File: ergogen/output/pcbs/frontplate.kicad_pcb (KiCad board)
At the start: 2 copper layers, 133.7 x 92.5 mm, 0 parts

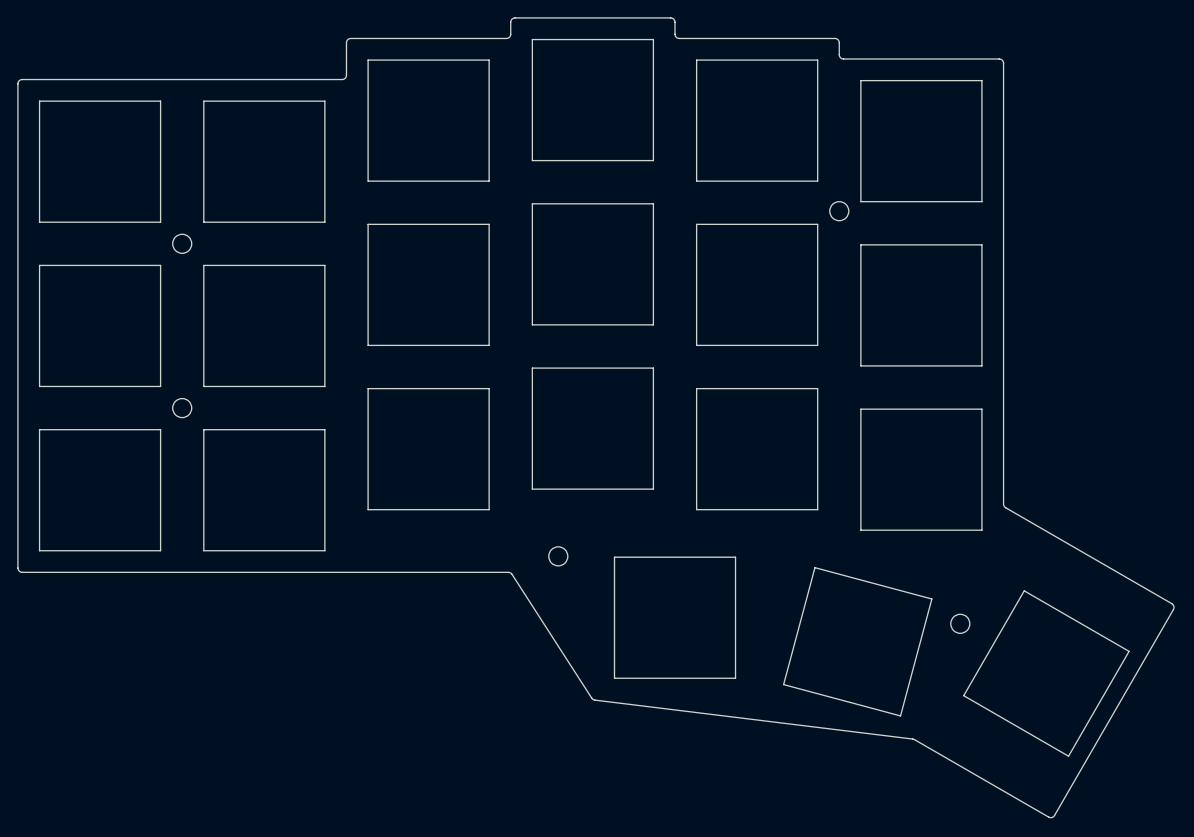
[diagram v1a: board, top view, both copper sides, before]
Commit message: Fix key positions to exactly match the corne
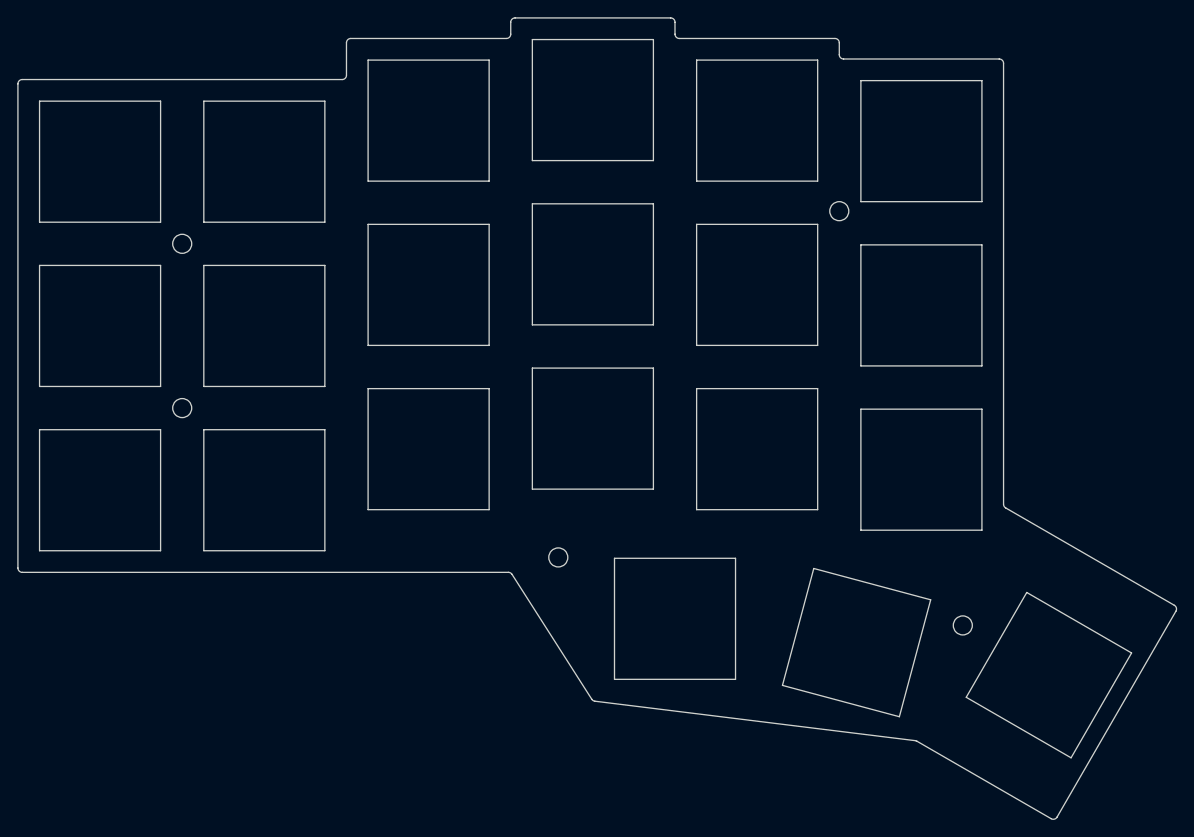
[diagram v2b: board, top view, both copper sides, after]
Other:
- board size 133.7 x 92.5 mm -> 134 x 92.7 mm
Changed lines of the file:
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@@
     (add_net "")
   )
-            (gr_line (start 91 109.5) (end 147.22730215593222 109.5) (angle 90) (layer Edge.Cuts) (width 0.15))
+            (gr_line (start 91 109.5) (end 147.226056907563 109.5) (angle 90) (layer Edge.Cuts) (width 0.15))
 (gr_line (start 90.5 109) (end 90.5 53) (angle 90) (layer Edge.Cuts) (width 0.15))
 (gr_line (start 91 52.5) (end 128 52.5) (angle 90) (layer Edge.Cuts) (width 0.15))
@@
 (gr_line (start 185.5 49.625) (end 185.5 48.25) (angle 90) (layer Edge.Cuts) (width 0.15))
 (gr_line (start 185 47.75) (end 167 47.75) (angle 90) (layer Edge.Cuts) (width 0.15))
-(gr_line (start 204.5 101.59766889781217) (end 204.5 50.625) (angle 90) (layer Edge.Cuts) (width 0.15))
+(gr_line (start 204.5 101.61675503683294) (end 204.5 50.625) (angle 90) (layer Edge.Cuts) (width 0.15))
 (gr_line (start 204 50.125) (end 186 50.125) (angle 90) (layer Edge.Cuts) (width 0.15))
-(gr_line (start 210.3979412988017 137.62313710032112) (end 224.14794130032098 113.80743850119836) (angle 90) (layer Edge.Cuts) (width 0.15))
-(gr_line (start 204.75 102.03068159781219) (end 223.96492860032103 113.12442580119826) (angle 90) (layer Edge.Cuts) (width 0.15))
-(gr_line (start 194.19299154809863 128.84455526290066) (end 209.71492859880163 137.80614980032107) (angle 90) (layer Edge.Cuts) (width 0.15))
-(gr_line (start 147.6476597559322 109.72926120000002) (end 156.8730776751543 124.05293639037114) (angle 90) (layer Edge.Cuts) (width 0.15))
-(gr_line (start 157.2326620183834 124.27849049566476) (end 194.00376480486958 128.78127505760708) (angle 90) (layer Edge.Cuts) (width 0.15))
-(gr_arc (start 147.22730215593222 110) (end 147.6476597559322 109.7292612) (angle -57.2157184809877) (layer Edge.Cuts) (width 0.15))
-(gr_arc (start 157.2934352751543 123.78219759037117) (end 156.87307767515432 124.05293639037117) (angle -50.23435431888237) (layer Edge.Cuts) (width 0.15))
-(gr_arc (start 193.94299154809863 129.27756796290063) (end 194.19299154809863 128.84455526290063) (angle -23.01863594630671) (layer Edge.Cuts) (width 0.15))
-(gr_arc (start 209.96492859880166 137.37313710032106) (end 209.71492859880166 137.80614980032107) (angle -89.99999999999889) (layer Edge.Cuts) (width 0.15))
-(gr_arc (start 223.714928600321 113.5574385011983) (end 224.147941300321 113.8074385011983) (angle -90.00000000000685) (layer Edge.Cuts) (width 0.15))
-(gr_arc (start 205 101.59766889781217) (end 204.5 101.59766889781217) (angle -59.99999989158499) (layer Edge.Cuts) (width 0.15))
+(gr_line (start 210.68768509880175 137.80950690032108) (end 224.43768510032112 113.99380830119821) (angle 90) (layer Edge.Cuts) (width 0.15))
+(gr_line (start 204.75000000000003 102.04976773683296) (end 224.25467240032103 113.31079560119827) (angle 90) (layer Edge.Cuts) (width 0.15))
+(gr_line (start 194.4825814717975 129.0308362223767) (end 210.00467239880174 137.99251960032112) (angle 90) (layer Edge.Cuts) (width 0.15))
+(gr_line (start 147.6474496930774 109.73087517731855) (end 156.87331650010177 124.17664030936987) (angle 90) (layer Edge.Cuts) (width 0.15))
+(gr_line (start 157.23359753636308 124.40376678062299) (end 194.2936932210506 128.9675976284421) (angle 90) (layer Edge.Cuts) (width 0.15))
+(gr_arc (start 147.226056907563 110) (end 147.647449607563 109.7308752) (angle -57.4354397170889) (layer Edge.Cuts) (width 0.15))
+(gr_arc (start 157.2947092856161 123.90751548668835) (end 156.8733165856161 124.17664028668835) (angle -50.414995185869486) (layer Edge.Cuts) (width 0.15))
+(gr_arc (start 194.23258147179752 129.4638489223767) (end 194.48258147179752 129.0308362223767) (angle -22.979555577197353) (layer Edge.Cuts) (width 0.15))
+(gr_arc (start 210.25467239880174 137.5595069003211) (end 210.00467239880174 137.99251960032112) (angle -90.00000000000279) (layer Edge.Cuts) (width 0.15))
+(gr_arc (start 224.00467240032108 113.74380830119827) (end 224.4376851003211 113.99380830119827) (angle -89.99999999999831) (layer Edge.Cuts) (width 0.15))
+(gr_arc (start 205 101.61675503683294) (end 204.5 101.61675503683294) (angle -59.999999891587805) (layer Edge.Cuts) (width 0.15))
 (gr_arc (start 204 50.625) (end 204.5 50.625) (angle -90) (layer Edge.Cuts) (width 0.15))
 (gr_arc (start 186 49.625) (end 185.5 49.625) (angle -90) (layer Edge.Cuts) (width 0.15))
@@
 (gr_line (start 202 52.625) (end 188 52.625) (angle 90) (layer Edge.Cuts) (width 0.15))
 (gr_line (start 188 52.625) (end 188 66.625) (angle 90) (layer Edge.Cuts) (width 0.15))
-(gr_line (start 159.5 121.75) (end 173.5 121.75) (angle 90) (layer Edge.Cuts) (width 0.15))
-(gr_line (start 173.5 121.75) (end 173.5 107.75) (angle 90) (layer Edge.Cuts) (width 0.15))
-(gr_line (start 173.5 107.75) (end 159.5 107.75) (angle 90) (layer Edge.Cuts) (width 0.15))
-(gr_line (start 159.5 107.75) (end 159.5 121.75) (angle 90) (layer Edge.Cuts) (width 0.15))
-(gr_line (start 179.0618622 122.4822331) (end 192.5848238 126.1056997) (angle 90) (layer Edge.Cuts) (width 0.15))
-(gr_line (start 192.5848238 126.1056997) (end 196.2082904 112.5827381) (angle 90) (layer Edge.Cuts) (width 0.15))
-(gr_line (start 196.2082904 112.5827381) (end 182.6853288 108.9592715) (angle 90) (layer Edge.Cuts) (width 0.15))
-(gr_line (start 182.6853288 108.9592715) (end 179.0618622 122.4822331) (angle 90) (layer Edge.Cuts) (width 0.15))
-(gr_line (start 212.01923979999998 130.7649656) (end 219.01923979999998 118.64061000000001) (angle 90) (layer Edge.Cuts) (width 0.15))
-(gr_line (start 219.01923979999998 118.64061000000001) (end 206.89488419999998 111.64061000000001) (angle 90) (layer Edge.Cuts) (width 0.15))
-(gr_line (start 206.89488419999998 111.64061000000001) (end 199.89488419999998 123.76496560000001) (angle 90) (layer Edge.Cuts) (width 0.15))
-(gr_line (start 199.89488419999998 123.76496560000001) (end 212.01923979999998 130.7649656) (angle 90) (layer Edge.Cuts) (width 0.15))
+(gr_line (start 159.5 121.875) (end 173.5 121.875) (angle 90) (layer Edge.Cuts) (width 0.15))
+(gr_line (start 173.5 121.875) (end 173.5 107.875) (angle 90) (layer Edge.Cuts) (width 0.15))
+(gr_line (start 173.5 107.875) (end 159.5 107.875) (angle 90) (layer Edge.Cuts) (width 0.15))
+(gr_line (start 159.5 107.875) (end 159.5 121.875) (angle 90) (layer Edge.Cuts) (width 0.15))
+(gr_line (start 178.9267859 122.5747475) (end 192.4497475 126.1982141) (angle 90) (layer Edge.Cuts) (width 0.15))
+(gr_line (start 192.4497475 126.1982141) (end 196.0732141 112.6752525) (angle 90) (layer Edge.Cuts) (width 0.15))
+(gr_line (start 196.0732141 112.6752525) (end 182.5502525 109.0517859) (angle 90) (layer Edge.Cuts) (width 0.15))
+(gr_line (start 182.5502525 109.0517859) (end 178.9267859 122.5747475) (angle 90) (layer Edge.Cuts) (width 0.15))
+(gr_line (start 212.3089836 130.9513354) (end 219.3089836 118.8269798) (angle 90) (layer Edge.Cuts) (width 0.15))
+(gr_line (start 219.3089836 118.8269798) (end 207.184628 111.8269798) (angle 90) (layer Edge.Cuts) (width 0.15))
+(gr_line (start 207.184628 111.8269798) (end 200.184628 123.9513354) (angle 90) (layer Edge.Cuts) (width 0.15))
+(gr_line (start 200.184628 123.9513354) (end 212.3089836 130.9513354) (angle 90) (layer Edge.Cuts) (width 0.15))
 (gr_circle (center 109.5 71.5) (end 110.6 71.5) (layer Edge.Cuts) (width 0.15))
 (gr_circle (center 109.5 90.5) (end 110.6 90.5) (layer Edge.Cuts) (width 0.15))
 (gr_circle (center 185.5 67.725) (end 186.6 67.725) (layer Edge.Cuts) (width 0.15))
-(gr_circle (center 153 107.65) (end 154.1 107.65) (layer Edge.Cuts) (width 0.15))
-(gr_circle (center 199.49776989999998 115.4527878) (end 200.59776989999997 115.4527878) (layer Edge.Cuts) (width 0.15))
+(gr_circle (center 153 107.775) (end 154.1 107.775) (layer Edge.Cuts) (width 0.15))
+(gr_circle (center 199.7875137 115.6391576) (end 200.8875137 115.6391576) (layer Edge.Cuts) (width 0.15))
 )

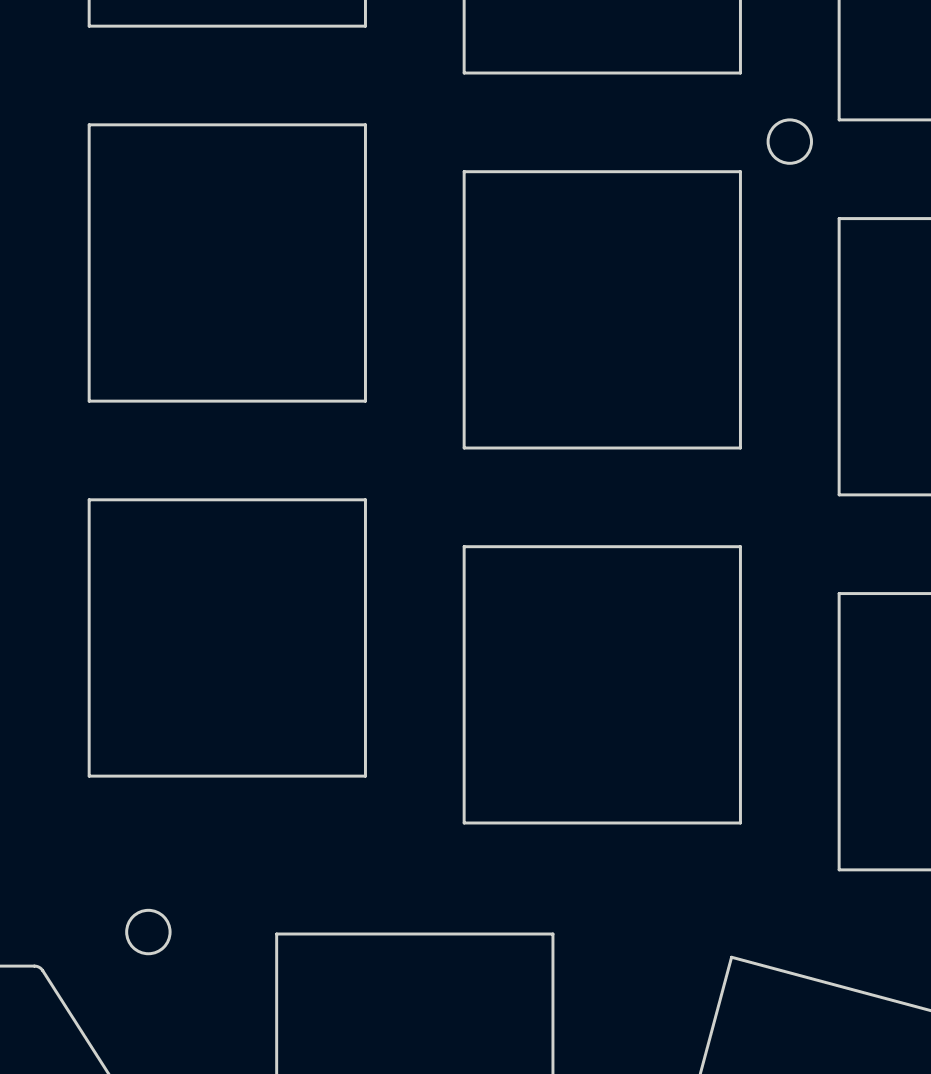
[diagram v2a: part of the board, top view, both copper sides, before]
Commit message: Fix MCU cover mounting holes position
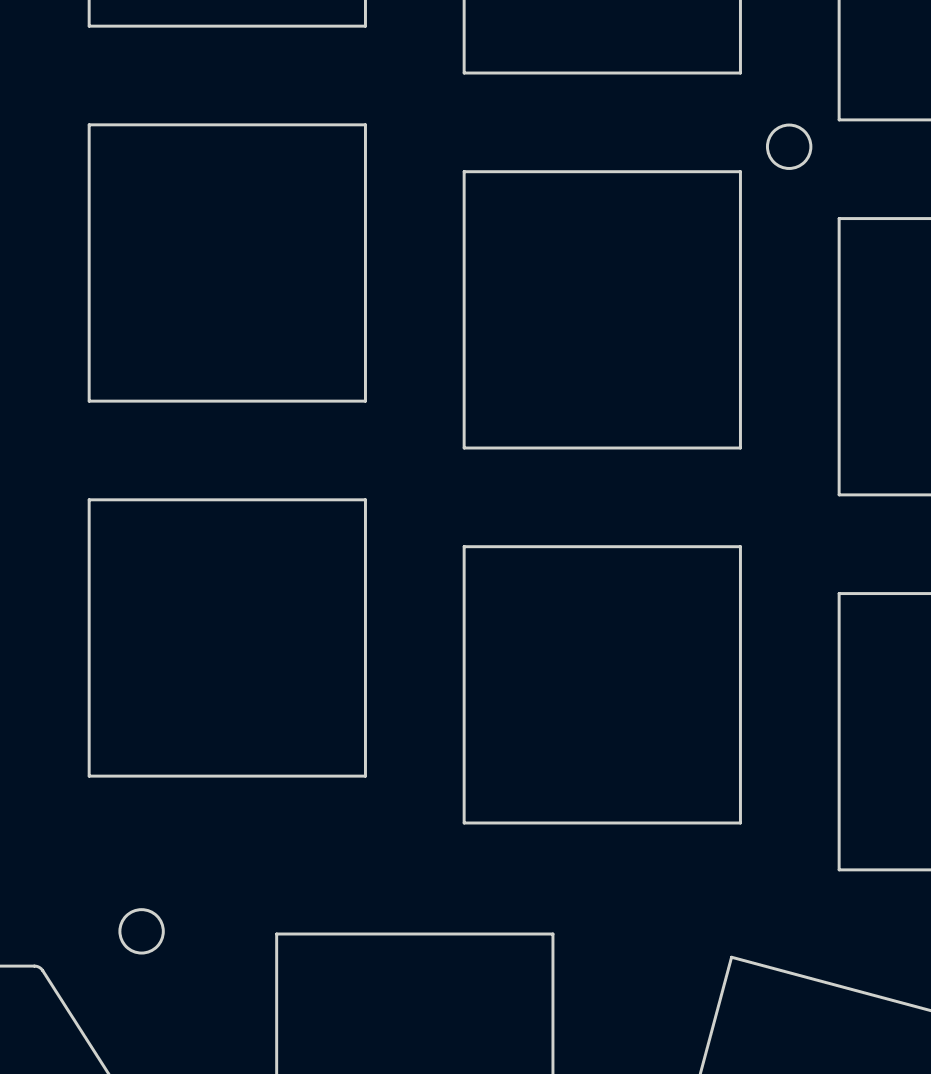
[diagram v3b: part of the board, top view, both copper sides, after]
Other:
- outline, holes or cut-outs redrawn
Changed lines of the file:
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@@
 (gr_circle (center 109.5 71.5) (end 110.6 71.5) (layer Edge.Cuts) (width 0.15))
 (gr_circle (center 109.5 90.5) (end 110.6 90.5) (layer Edge.Cuts) (width 0.15))
-(gr_circle (center 185.5 67.725) (end 186.6 67.725) (layer Edge.Cuts) (width 0.15))
-(gr_circle (center 153 107.775) (end 154.1 107.775) (layer Edge.Cuts) (width 0.15))
+(gr_circle (center 185.468 67.986) (end 186.56799999999998 67.986) (layer Edge.Cuts) (width 0.15))
+(gr_circle (center 152.657 107.74) (end 153.757 107.74) (layer Edge.Cuts) (width 0.15))
 (gr_circle (center 199.7875137 115.6391576) (end 200.8875137 115.6391576) (layer Edge.Cuts) (width 0.15))
 )

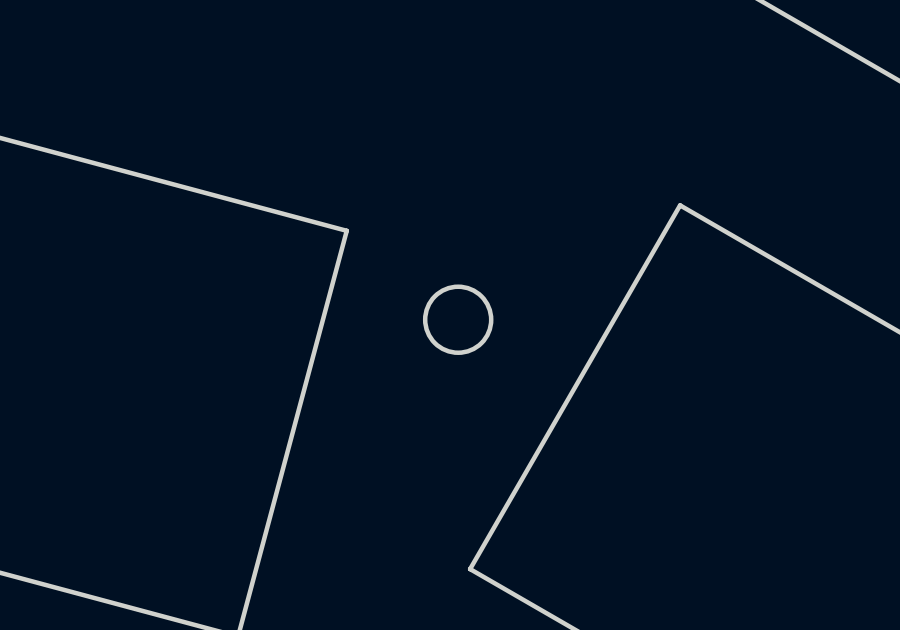
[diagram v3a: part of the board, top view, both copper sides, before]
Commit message: Fix inner underglow LED position
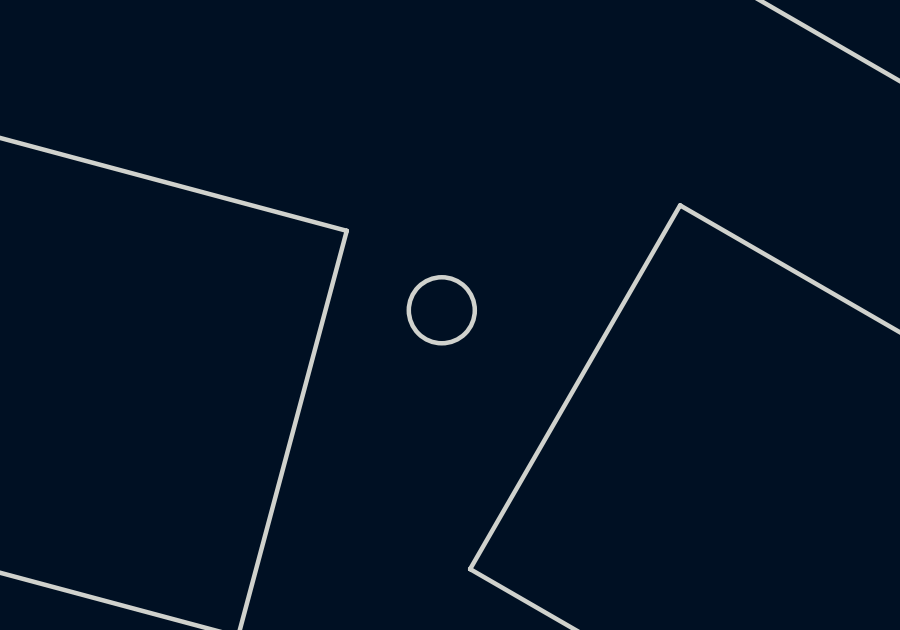
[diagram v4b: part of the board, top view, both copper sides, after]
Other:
- outline, holes or cut-outs redrawn
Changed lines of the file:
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@@
 (gr_circle (center 185.468 67.986) (end 186.56799999999998 67.986) (layer Edge.Cuts) (width 0.15))
 (gr_circle (center 152.657 107.74) (end 153.757 107.74) (layer Edge.Cuts) (width 0.15))
-(gr_circle (center 199.7875137 115.6391576) (end 200.8875137 115.6391576) (layer Edge.Cuts) (width 0.15))
+(gr_circle (center 199.2410516 115.3236576) (end 200.3410516 115.3236576) (layer Edge.Cuts) (width 0.15))
 )
